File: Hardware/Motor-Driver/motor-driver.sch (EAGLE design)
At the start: 48 parts, among them U1 STM32-M-64-LQFP, U2 MIC5233-5.0YM5-TR, U3 MIC5233-3.3YM5-TR, U4 TJA1042HVSON, U5 MIC5233-5.0YM5-TR, U6 MCP6002, Y1 16MHz

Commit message: new boards
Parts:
- removed C26: 100nF, comma.ai:C0603
- removed R1, R2, R3, R4, R7, R8: 10k, comma.ai:R0402
- removed R23, R24, R25, R26: 1k, comma.ai:R0402
- removed SJ1: (no value), jumper:SJ2W
- removed U$1, U$3: MICROFIT-6, interceptor:MICROFIT-6
- removed U6: MCP6002, comma.ai:LM358D
- added SWD: (no value), SparkFun-Connectors:CONN_051.27MM
- C1: value 2.2uF -> 4.7u
- C12: value 4.7uF -> 2.2u
- C2: value 2.2uF -> 2.2u
- U5: value MIC5233-5.0YM5-TR -> Value; device SamacSys_Parts:MIC5233-5.0YM5-TR -> comma.ai:DRV8873HPWPRQ1
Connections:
- removed net ACCEL1: R23.2, U$3.2
- removed net ACCEL2: R24.2, U$3.5
- removed net DAC1: R3.2, U$1.2, U6A.OUT
- removed net DAC2: R2.2, U$1.5, U6B.OUT
- removed net DACV: C26.1, U$1.3, U$1.6, U6P.V+
- removed net N$10: R6.2, S1.2, U1.NRST
- removed net N$14: SJ1.1, U5.OUT
- removed net N$17: R7.2, U1.PA4-SPI1NSS/ADC4/USART2CK/DAC_OUT1, U6A.+IN
- removed net N$18: R8.2, U1.PA5-SPI1SCK/ADC5/DAC_OUT2, U6B.+IN
- removed net N$21: R1.2, R3.1, U6A.-IN
- removed net N$22: R2.1, R4.2, U6B.-IN
- removed net N$41: R23.1, R26.1, U1.PC0-ADC10
- removed net N$42: R24.1, R25.1, U1.PC1-ADC11
- new net N$13: SWD.4, U1.PA13/JTMS/SWDIO
- new net NRST: R6.2, S1.2, SWD.2, U1.NRST
- net 3V3: now also C1.1, SWD.5; no longer C12.1
- net 5V: no longer SJ1.3, U$3.3, U5.EN, U5.IN
- net GND: now also C2.2, SWD.1; no longer C2.1, C26.2, R1.1, R25.2, R26.2, R4.1, R7.1, R8.1, U$1.1, U$1.4, U$3.1, U$3.4, U5.GND, U6P.V-, Y1.3
- net N$12: now also SWD.3, U1.PA14/JTCK/SWCLK; no longer SJ1.2, U$3.6
- net VCAP1: now also C12.1; no longer C2.2
- net VCAP2: now also C2.1; no longer C1.1
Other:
- note removed: "*"
- note removed: "*0.1% precision"
- moved on the sheet: C1, C10, C11, C12, C13, C14, C2, C3, C4, C5, C6, C7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

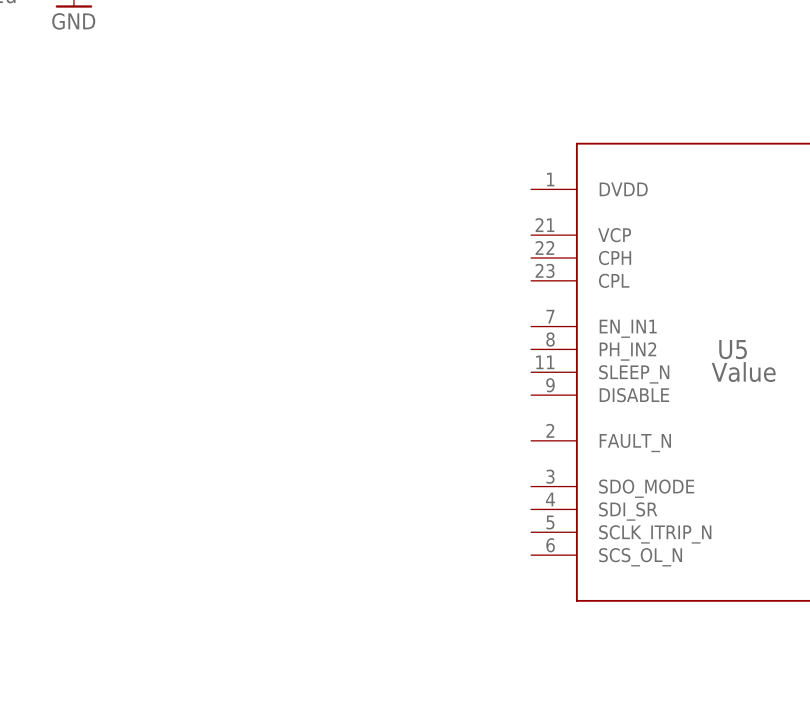
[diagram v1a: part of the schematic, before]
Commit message: ibooster v2, stm32teensy work
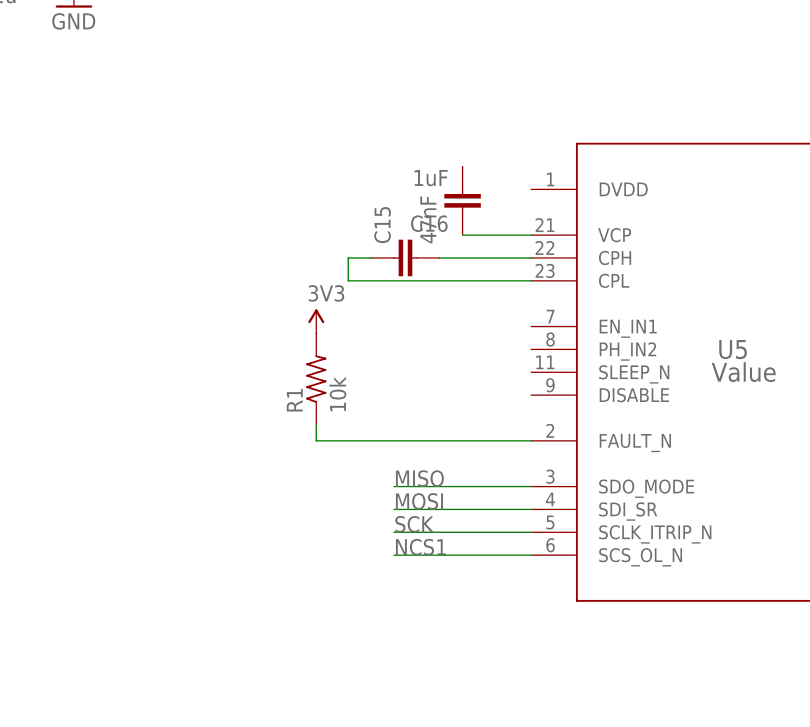
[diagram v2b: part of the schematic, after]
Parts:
- added C15: 47nF, comma.ai:C0603
- added C16: 1uF, comma.ai:C0603
- added R1: 10k, comma.ai:R0402
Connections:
- new net MISO: U5.SDO_MODE
- new net MOSI: U5.SDI_SR
- new net N$10: C15.2, U5.CPH
- new net N$14: C15.1, U5.CPL
- new net N$15: C16.1, U5.VCP
- new net N$16: R1.1, U5.FAULT_N
- new net NCS1: U5.SCS_OL_N
- new net SCK: U5.SCLK_ITRIP_N
- new net VCC: R1.2
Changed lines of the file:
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@@
 <part name="GND10" library="SparkFun-Aesthetics" library_urn="urn:adsk.eagle:library:507" deviceset="GND" device=""/>
 <part name="U5" library="comma.ai" deviceset="DRV8873HPWPRQ1" device="" value="Value"/>
+<part name="C15" library="comma.ai" deviceset="C" device="0603" value="47nF"/>
+<part name="C16" library="comma.ai" deviceset="C" device="0603" value="1uF"/>
+<part name="R1" library="comma.ai" deviceset="R" device="0402" value="10k"/>
+<part name="SUPPLY4" library="SparkFun-Aesthetics" library_urn="urn:adsk.eagle:library:507" deviceset="VCC" device="" value="3V3"/>
 </parts>
 <sheets>
@@
 <attribute name="VALUE" x="345.1606" y="95.4786" size="2.0828" layer="96" ratio="6" rot="SR0"/>
 <attribute name="VALUE" x="345.1606" y="95.4786" size="2.0828" layer="96" ratio="6" rot="SR0"/>
+</instance>
+<instance part="C15" gate="G$1" x="312.42" y="109.22" smashed="yes" rot="R90">
+<attribute name="NAME" x="309.499" y="110.744" size="1.778" layer="95" rot="R90"/>
+<attribute name="VALUE" x="314.579" y="110.744" size="1.778" layer="96" rot="R90"/>
+</instance>
+<instance part="C16" gate="G$1" x="317.5" y="116.84" smashed="yes" rot="R180">
+<attribute name="NAME" x="315.976" y="113.919" size="1.778" layer="95" rot="R180"/>
+<attribute name="VALUE" x="315.976" y="118.999" size="1.778" layer="96" rot="R180"/>
+</instance>
+<instance part="R1" gate="G$1" x="301.244" y="95.758" smashed="yes" rot="R90">
+<attribute name="NAME" x="299.7454" y="91.948" size="1.778" layer="95" rot="R90"/>
+<attribute name="VALUE" x="304.546" y="91.948" size="1.778" layer="96" rot="R90"/>
+</instance>
+<instance part="SUPPLY4" gate="G$1" x="301.244" y="100.838" smashed="yes">
+<attribute name="VALUE" x="300.228" y="104.394" size="1.778" layer="96"/>
 </instance>
 </instances>
@@
 </segment>
 </net>
+<net name="N$10" class="0">
+<segment>
+<pinref part="C15" gate="G$1" pin="2"/>
+<pinref part="U5" gate="A" pin="CPH"/>
+<wire x1="314.96" y1="109.22" x2="325.12" y2="109.22" width="0.1524" layer="91"/>
+</segment>
+</net>
+<net name="N$14" class="0">
+<segment>
+<pinref part="U5" gate="A" pin="CPL"/>
+<wire x1="325.12" y1="106.68" x2="304.8" y2="106.68" width="0.1524" layer="91"/>
+<wire x1="304.8" y1="106.68" x2="304.8" y2="109.22" width="0.1524" layer="91"/>
+<pinref part="C15" gate="G$1" pin="1"/>
+<wire x1="304.8" y1="109.22" x2="307.34" y2="109.22" width="0.1524" layer="91"/>
+</segment>
+</net>
+<net name="N$15" class="0">
+<segment>
+<pinref part="U5" gate="A" pin="VCP"/>
+<pinref part="C16" gate="G$1" pin="1"/>
+<wire x1="325.12" y1="111.76" x2="317.5" y2="111.76" width="0.1524" layer="91"/>
+</segment>
+</net>
+<net name="N$16" class="0">
+<segment>
+<pinref part="U5" gate="A" pin="FAULT_N"/>
+<wire x1="325.12" y1="88.9" x2="301.244" y2="88.9" width="0.1524" layer="91"/>
+<pinref part="R1" gate="G$1" pin="1"/>
+<wire x1="301.244" y1="88.9" x2="301.244" y2="90.678" width="0.1524" layer="91"/>
+</segment>
+</net>
+<net name="VCC" class="0">
+<segment>
+<pinref part="R1" gate="G$1" pin="2"/>
+<pinref part="SUPPLY4" gate="G$1" pin="VCC"/>
+</segment>
+</net>
+<net name="MISO" class="0">
+<segment>
+<pinref part="U5" gate="A" pin="SDO_MODE"/>
+<wire x1="325.12" y1="83.82" x2="309.88" y2="83.82" width="0.1524" layer="91"/>
+<label x="309.88" y="83.82" size="1.778" layer="95"/>
+</segment>
+</net>
+<net name="MOSI" class="0">
+<segment>
+<pinref part="U5" gate="A" pin="SDI_SR"/>
+<wire x1="325.12" y1="81.28" x2="309.88" y2="81.28" width="0.1524" layer="91"/>
+<label x="309.88" y="81.28" size="1.778" layer="95"/>
+</segment>
+</net>
+<net name="SCK" class="0">
+<segment>
+<pinref part="U5" gate="A" pin="SCLK_ITRIP_N"/>
+<wire x1="325.12" y1="78.74" x2="309.88" y2="78.74" width="0.1524" layer="91"/>
+<label x="309.88" y="78.74" size="1.778" layer="95"/>
+</segment>
+</net>
+<net name="NCS1" class="0">
+<segment>
+<pinref part="U5" gate="A" pin="SCS_OL_N"/>
+<wire x1="325.12" y1="76.2" x2="309.88" y2="76.2" width="0.1524" layer="91"/>
+<label x="309.88" y="76.2" size="1.778" layer="95"/>
+</segment>
+</net>
